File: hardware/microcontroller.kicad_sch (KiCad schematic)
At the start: 15 parts, among them J5 1x2 jumper right-angle, J7 1x2 jumper right-angle, U16 3.3V <=> 5V, U17 decoder

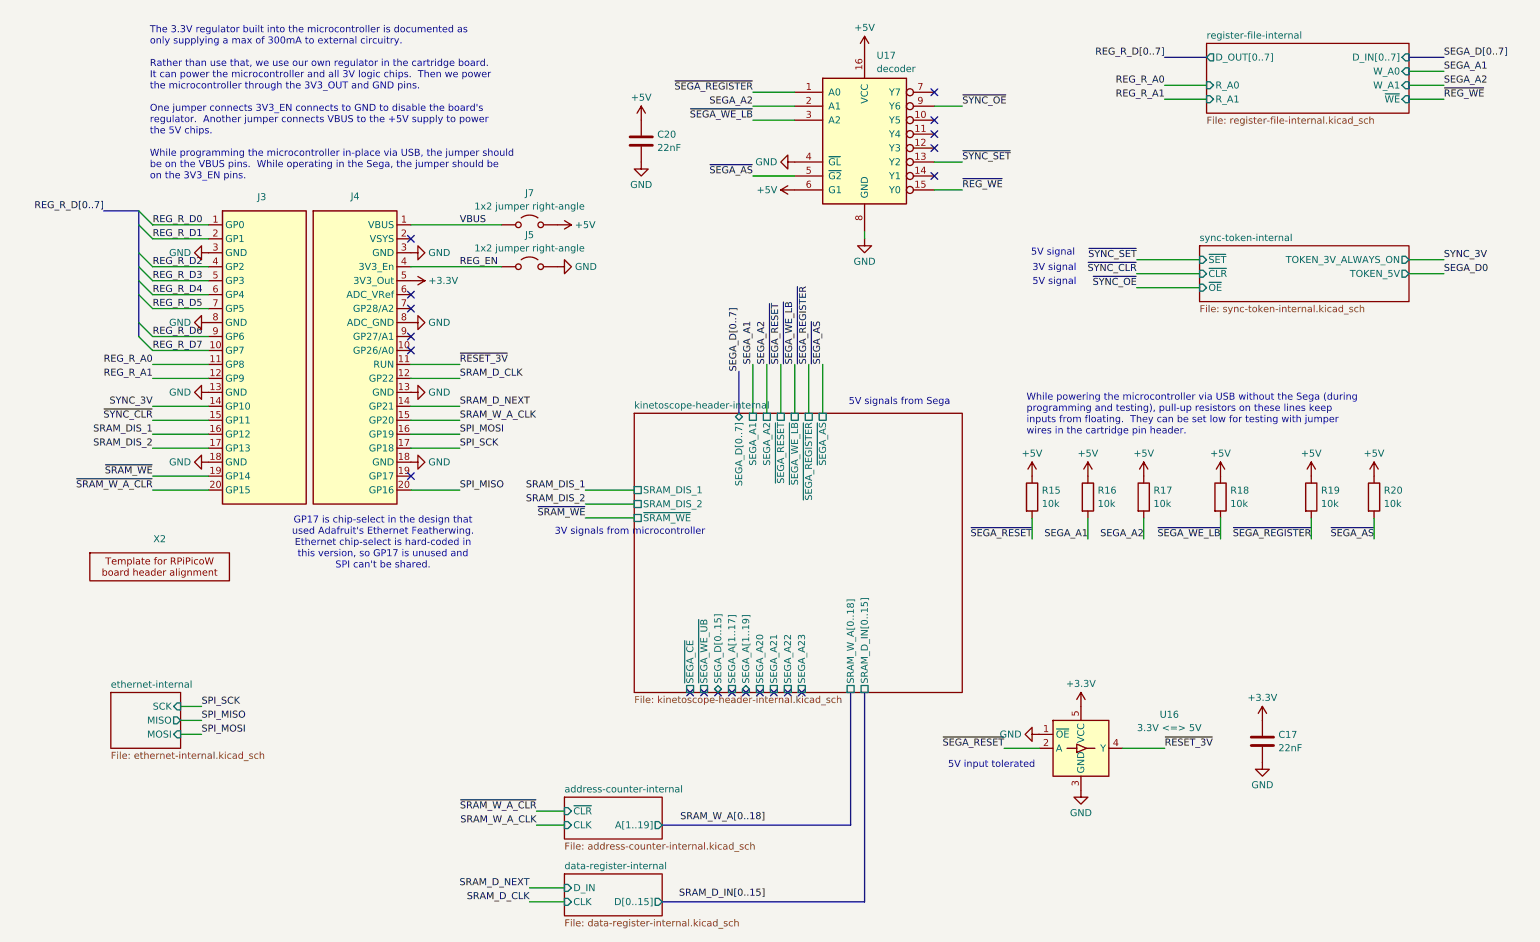
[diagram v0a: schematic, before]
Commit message: Fix ethernet chip-select and register address decoder
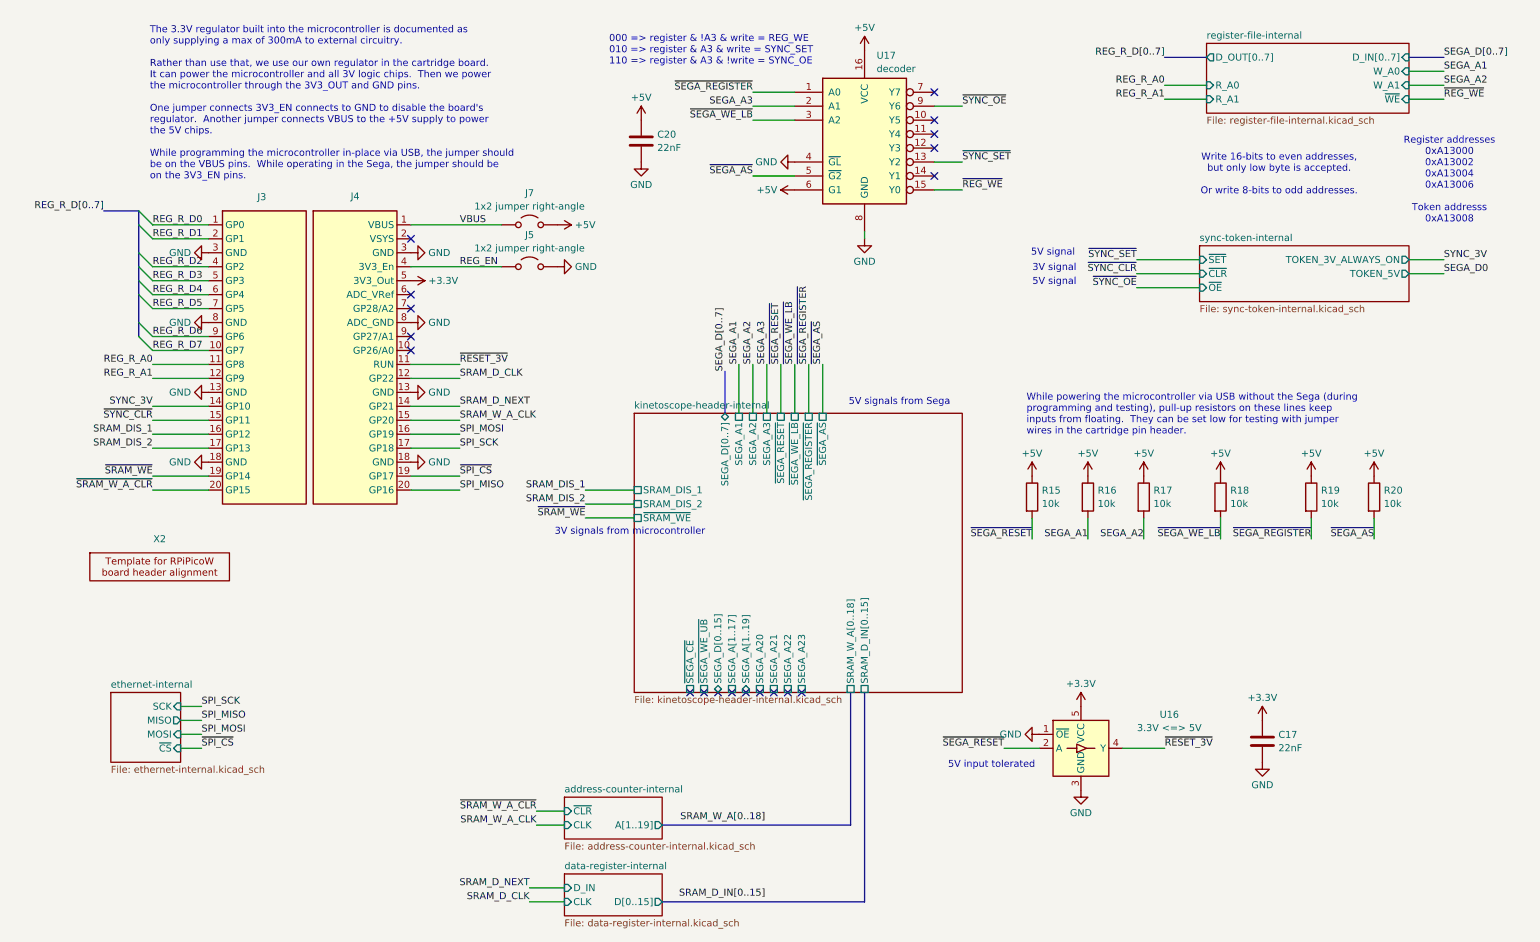
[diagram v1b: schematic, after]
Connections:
- net SEGA_A2: no longer U17.2 (A1)
- net ~{SPI_CS}: now reaches J4.19 (GP17)
- new net SEGA_A3: U17.2 (A1)
- no-connect marks 20 -> 19
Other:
- sheet ethernet-internal ports: added ~{CS}; removed none
- sheet kinetoscope-header-internal ports: added SEGA_A3; removed none
- note added: "000 => register & !A3 & write = REG_WE 010 => register & A3 & write = SYNC_SET 110 => register & A3 & !write = SYNC_OE"
- note added: "Register addresses 0xA13000 0xA13002 0xA13004 0xA13006 Token addresss 0xA13008"
- note added: "Write 16-bits to even addresses, but only low byte is accepted. Or write 8-bits to odd addresses."
- note removed: "GP17 is chip-select in the design that used Adafruit's Ethernet Featherwing. Ethernet chip-select is hard-coded in this version, so GP17 is unused and SPI can't be shared."
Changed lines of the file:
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@@
 	)
 	(no_connect
-		(at 82.55 96.52)
-	)
-	(no_connect
 		(at 177.8 36.83)
 	)
@@
 	(wire
 		(pts
-			(xy 35.56 99.06) (xy 45.72 99.06)
+			(xy 147.32 76.2) (xy 147.32 85.09)
 		)
 		(stroke
@@
 	(wire
 		(pts
-			(xy 270.51 57.15) (xy 264.16 57.15)
+			(xy 35.56 99.06) (xy 45.72 99.06)
 		)
 		(stroke
@@
 	(wire
 		(pts
-			(xy 147.32 76.2) (xy 147.32 85.09)
+			(xy 270.51 57.15) (xy 264.16 57.15)
 		)
 		(stroke
@@
 		)
 	)
+	(bus
+		(pts
+			(xy 139.7 77.47) (xy 139.7 85.09)
+		)
+		(stroke
+			(width 0)
+			(type default)
+		)
+	)
 	(wire
 		(pts
@@
 		)
 	)
+	(wire
+		(pts
+			(xy 142.24 76.2) (xy 142.24 85.09)
+		)
+		(stroke
+			(width 0)
+			(type default)
+		)
+	)
 	(bus
 		(pts
@@
 	(wire
 		(pts
+			(xy 82.55 96.52) (xy 91.44 96.52)
+		)
+		(stroke
+			(width 0)
+			(type default)
+		)
+	)
+	(wire
+		(pts
 			(xy 35.56 78.74) (xy 45.72 78.74)
 		)
@@
 		)
 	)
-	(bus
-		(pts
-			(xy 142.24 77.47) (xy 142.24 85.09)
-		)
-		(stroke
-			(width 0)
-			(type default)
-		)
-	)
 	(wire
 		(pts
@@
 	(wire
 		(pts
-			(xy 144.78 29.21) (xy 152.4 29.21)
-		)
-		(stroke
-			(width 0)
-			(type default)
-		)
-	)
-	(wire
-		(pts
 			(xy 82.55 91.44) (xy 91.44 91.44)
 		)
@@
 	(wire
 		(pts
+			(xy 144.78 76.2) (xy 144.78 85.09)
+		)
+		(stroke
+			(width 0)
+			(type default)
+		)
+	)
+	(wire
+		(pts
 			(xy 219.71 25.4) (xy 227.33 25.4)
 		)
@@
 	(wire
 		(pts
+			(xy 40.64 146.05) (xy 44.45 146.05)
+		)
+		(stroke
+			(width 0)
+			(type default)
+		)
+	)
+	(wire
+		(pts
 			(xy 177.8 44.45) (xy 182.88 44.45)
 		)
@@
 	(wire
 		(pts
-			(xy 144.78 76.2) (xy 144.78 85.09)
-		)
-		(stroke
-			(width 0)
-			(type default)
-		)
-	)
-	(wire
-		(pts
 			(xy 35.56 71.12) (xy 45.72 71.12)
 		)
@@
 	(wire
 		(pts
+			(xy 144.78 29.21) (xy 152.4 29.21)
+		)
+		(stroke
+			(width 0)
+			(type default)
+		)
+	)
+	(wire
+		(pts
 			(xy 35.56 53.34) (xy 45.72 53.34)
 		)
@@
 		)
 	)
+	(text "Register addresses\n0xA13000\n0xA13002\n0xA13004\n0xA13006\n\nToken addresss\n0xA13008"
+		(exclude_from_sim no)
+		(at 271.526 42.672 0)
+		(effects
+			(font
+				(size 1.27 1.27)
+			)
+		)
+	)
 	(text "5V input tolerated"
 		(exclude_from_sim no)
@@
 		)
 	)
-	(text "GP17 is chip-select in the design that\nused Adafruit's Ethernet Featherwing.\nEthernet chip-select is hard-coded in\nthis version, so GP17 is unused and\nSPI can't be shared."
+	(text "000 => register & !A3 & write = REG_WE\n010 => register & A3 & write = SYNC_SET\n110 => register & A3 & !write = SYNC_OE"
 		(exclude_from_sim no)
-		(at 77.47 108.712 0)
+		(at 118.618 19.05 0)
 		(effects
 			(font
 				(size 1.27 1.27)
 			)
+			(justify left)
 		)
 	)
@@
 		)
 	)
+	(text "Write 16-bits to even addresses,\nbut only low byte is accepted.\n\nOr write 8-bits to odd addresses."
+		(exclude_from_sim no)
+		(at 240.538 41.656 0)
+		(effects
+			(font
+				(size 1.27 1.27)
+			)
+		)
+	)
 	(text "5V signal"
 		(exclude_from_sim no)
@@
 		)
 	)
+	(label "~{SPI_CS}"
+		(at 44.45 146.05 0)
+		(fields_autoplaced yes)
+		(effects
+			(font
+				(size 1.27 1.27)
+			)
+			(justify left bottom)
+		)
+	)
 	(label "~{SEGA_WE_LB}"
 		(at 229.87 107.95 180)
@@
 		)
 	)
+	(label "~{SPI_CS}"
+		(at 91.44 96.52 0)
+		(fields_autoplaced yes)
+		(effects
+			(font
+				(size 1.27 1.27)
+			)
+			(justify left bottom)
+		)
+	)
 	(label "REG_R_A0"
 		(at 35.56 76.2 180)
@@
 		)
 	)
-	(label "SEGA_A2"
+	(label "SEGA_A3"
 		(at 144.78 29.21 180)
 		(fields_autoplaced yes)
@@
 	)
 	(label "SEGA_A1"
-		(at 144.78 76.2 90)
+		(at 142.24 76.2 90)
 		(fields_autoplaced yes)
 		(effects
@@
 	)
 	(label "SEGA_A2"
-		(at 147.32 76.2 90)
+		(at 144.78 76.2 90)
 		(fields_autoplaced yes)
 		(effects
@@
 	)
 	(label "SEGA_D[0..7]"
-		(at 142.24 77.47 90)
+		(at 139.7 77.47 90)
 		(fields_autoplaced yes)
 		(effects
@@
 		)
 	)
+	(label "SEGA_A3"
+		(at 147.32 76.2 90)
+		(fields_autoplaced yes)
+		(effects
+			(font
+				(size 1.27 1.27)
+			)
+			(justify left bottom)
+		)
+	)
 	(label "SEGA_A1"
 		(at 205.74 107.95 180)
@@
 		)
 		(pin "SEGA_D[0..7]" bidirectional
-			(at 142.24 85.09 90)
+			(at 139.7 85.09 90)
 			(effects
 				(font
@@
 		)
 		(pin "SEGA_A2" passive
-			(at 147.32 85.09 90)
+			(at 144.78 85.09 90)
 			(effects
 				(font
@@
 		)
 		(pin "SEGA_A1" passive
-			(at 144.78 85.09 90)
+			(at 142.24 85.09 90)
+			(effects
+				(font
+					(size 1.27 1.27)
+				)
+				(justify right)
+			)
+		)
+		(pin "SEGA_A3" passive
+			(at 147.32 85.09 90)
 			(effects
 				(font
@@
 	(sheet
 		(at 27.94 135.89)
-		(size 12.7 10.16)
+		(size 12.7 12.7)
 		(fields_autoplaced yes)
 		(stroke
@@
 		)
 		(property "Sheetfile" "ethernet-internal.kicad_sch"
-			(at 27.94 146.6346 0)
+			(at 27.94 149.1746 0)
 			(effects
 				(font
@@
 			(effects
 				(font
+					(size 1.27 1.27)
+				)
+				(justify right)
+			)
+		)
+		(pin "~{CS}" input
+			(at 40.64 146.05 0)
+			(effects
+				(font

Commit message: Add second sync bit to flag errors back to the Sega
Also split firmware speed tests out into their own file
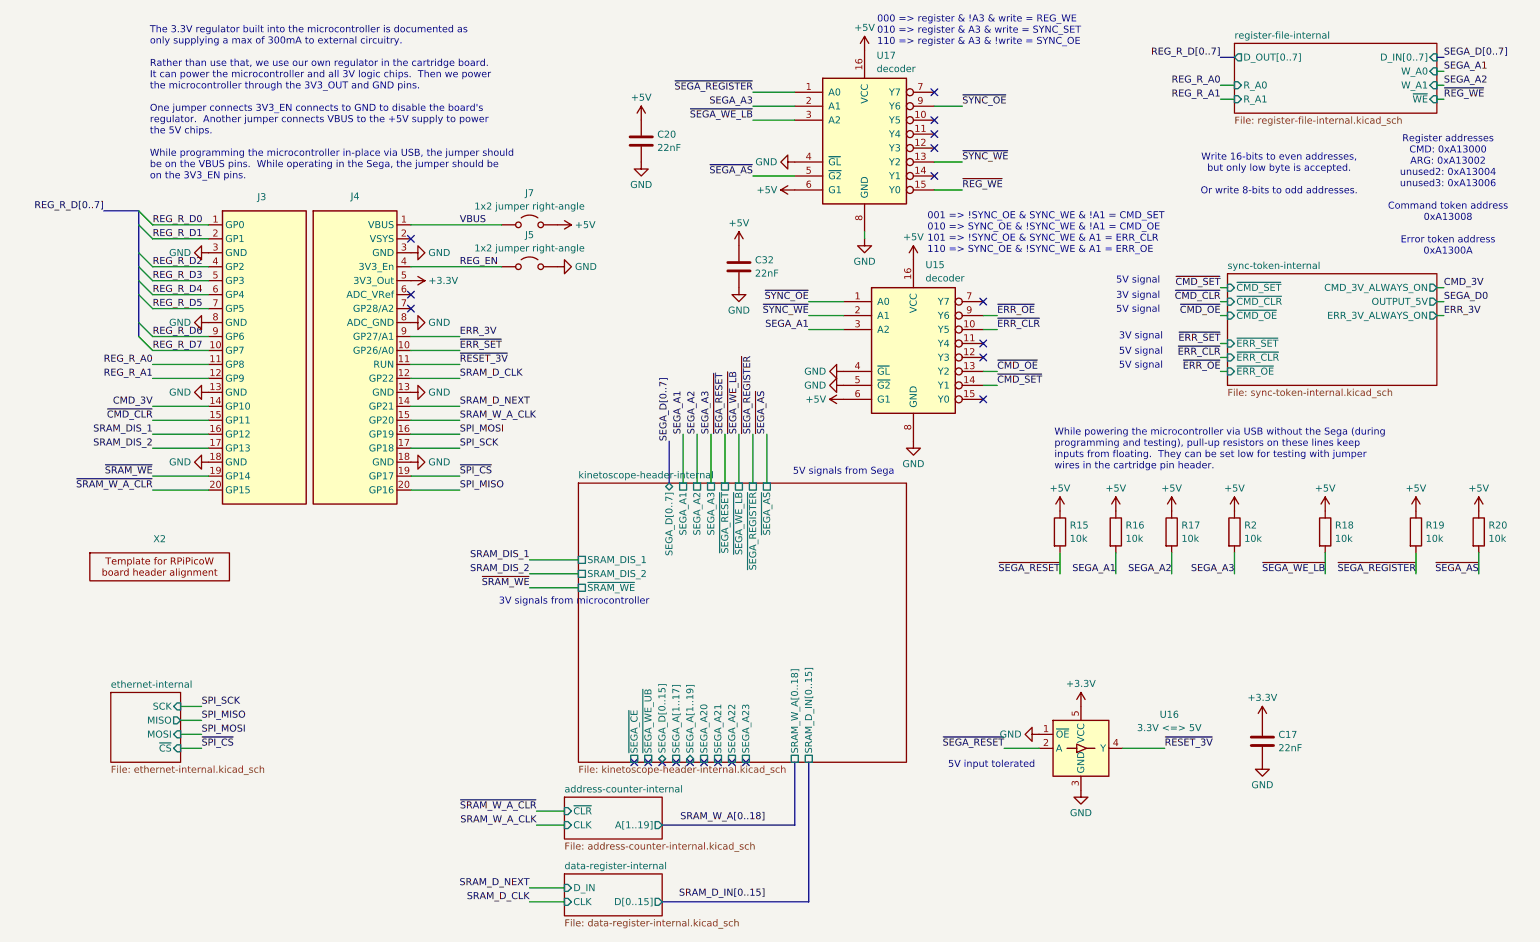
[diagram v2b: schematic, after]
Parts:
- added C32: 22nF, Capacitor_SMD:C_0603_1608Metric, symbol Device:C
- added R2: 10k, Resistor_SMD:R_0603_1608Metric, symbol Device:R
- added U15: decoder, Package_SO:SO-16_3.9x9.9mm_P1.27mm, symbol 74xx:74LS137
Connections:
- net +5V: now also C32.1, R2.1, U15.16 (VCC), U15.6 (G1)
- net GND: now also C32.2, U15.4 (~{GL}), U15.5 (~{G2}), U15.8 (GND)
- net SEGA_A1: now also U15.3 (A2)
- net SEGA_A3: now also R2.2
- net ~{SYNC_OE}: now also U15.1 (A0)
- net ~{ERR_SET}: now reaches J4.10 (GP26/A0)
- net ERR_3V: now reaches J4.9 (GP27/A1)
- net SYNC_3V renamed CMD_3V
- net ~{SYNC_CLR} renamed ~{CMD_CLR}
- net ~{SYNC_SET} renamed ~{SYNC_WE}
- net ~{SYNC_WE}: now also U15.2 (A1)
- new net ~{CMD_OE}: U15.13 (Y2)
- new net ~{CMD_SET}: U15.14 (Y1)
- new net ~{ERR_CLR}: U15.10 (Y5)
- new net ~{ERR_OE}: U15.9 (Y6)
- no-connect marks 19 -> 21
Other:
- sheet sync-token-internal ports: added CMD_3V_ALWAYS_ON, ERR_3V_ALWAYS_ON, OUTPUT_5V, ~{CMD_CLR}, ~{CMD_OE}, ~{CMD_SET}, ~{ERR_CLR}, ~{ERR_OE}, ~{ERR_SET}; removed TOKEN_3V_ALWAYS_ON, TOKEN_5V, ~{CLR}, ~{OE}, ~{SET}
- note added: "001 => !SYNC_OE & SYNC_WE & !A1 = CMD_SET 010 => SYNC_OE & !SYNC_WE & !A1 = CMD_OE 101 => !SYNC_OE & SYNC_WE & A1 = ERR_CLR 110 => SYNC_OE & !SYNC_WE & A1 = ERR_OE"
- note added: "Register addresses CMD: 0xA13000 ARG: 0xA13002 unused2: 0xA13004 unused3: 0xA13006 Command token address 0xA13008 Error token address 0xA1300A"
- note removed: "Register addresses 0xA13000 0xA13002 0xA13004 0xA13006 Token addresss 0xA13008"
- moved on the sheet: R15, R16, R17, R18, R19, R20

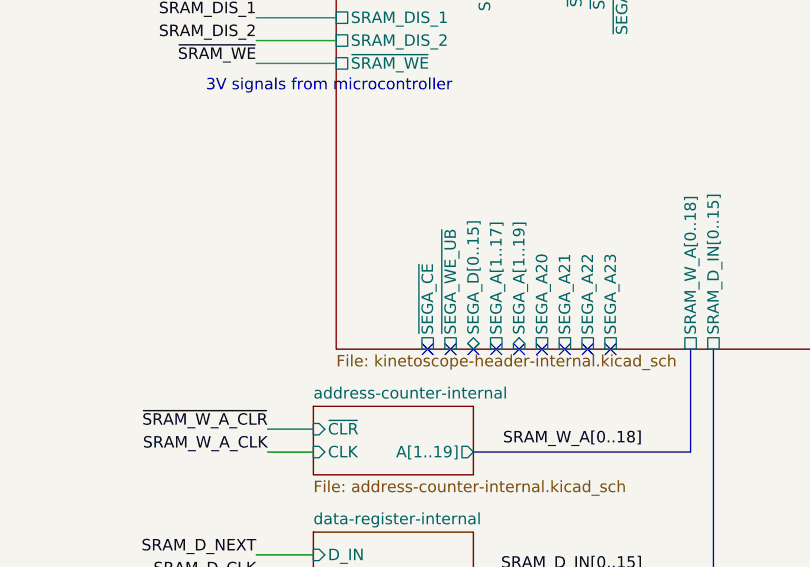
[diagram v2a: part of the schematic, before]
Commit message: Update interboard header in microcontroller and SRAM boards
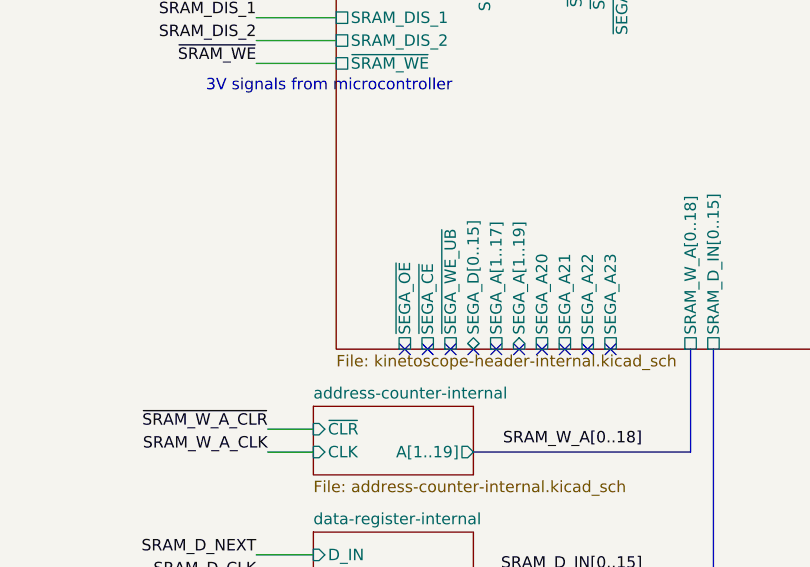
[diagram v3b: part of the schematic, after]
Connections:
- no-connect marks 21 -> 22
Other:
- sheet kinetoscope-header-internal ports: added ~{SEGA_OE}; removed none
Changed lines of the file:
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@@
 	)
 	(no_connect
+		(at 120.65 148.59)
+	)
+	(no_connect
 		(at 186.69 82.55)
 	)
@@
 			)
 		)
+		(pin "~{SEGA_OE}" passive
+			(at 120.65 148.59 270)
+			(effects
+				(font
+					(size 1.27 1.27)
+				)
+				(justify left)
+			)
+		)
